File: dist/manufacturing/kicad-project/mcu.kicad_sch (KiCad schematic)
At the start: 22 parts, among them SW1 SW1, U16 STM32G0B1CBT6, U17 W25Q32JVSSIQ, Y1 Y1

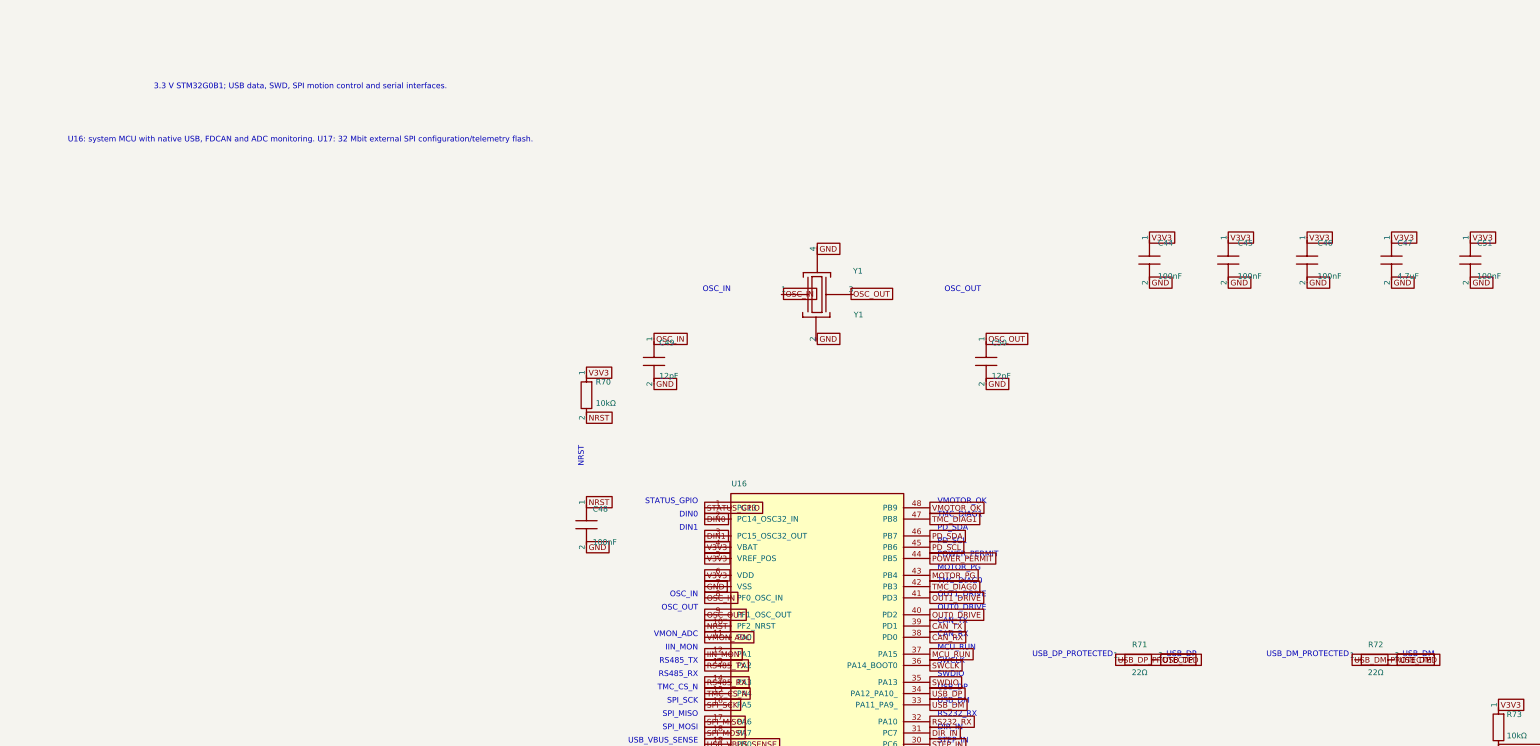
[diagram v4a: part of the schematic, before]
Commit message: Implement dual USB power/data ECO and consolidate industrial I/O
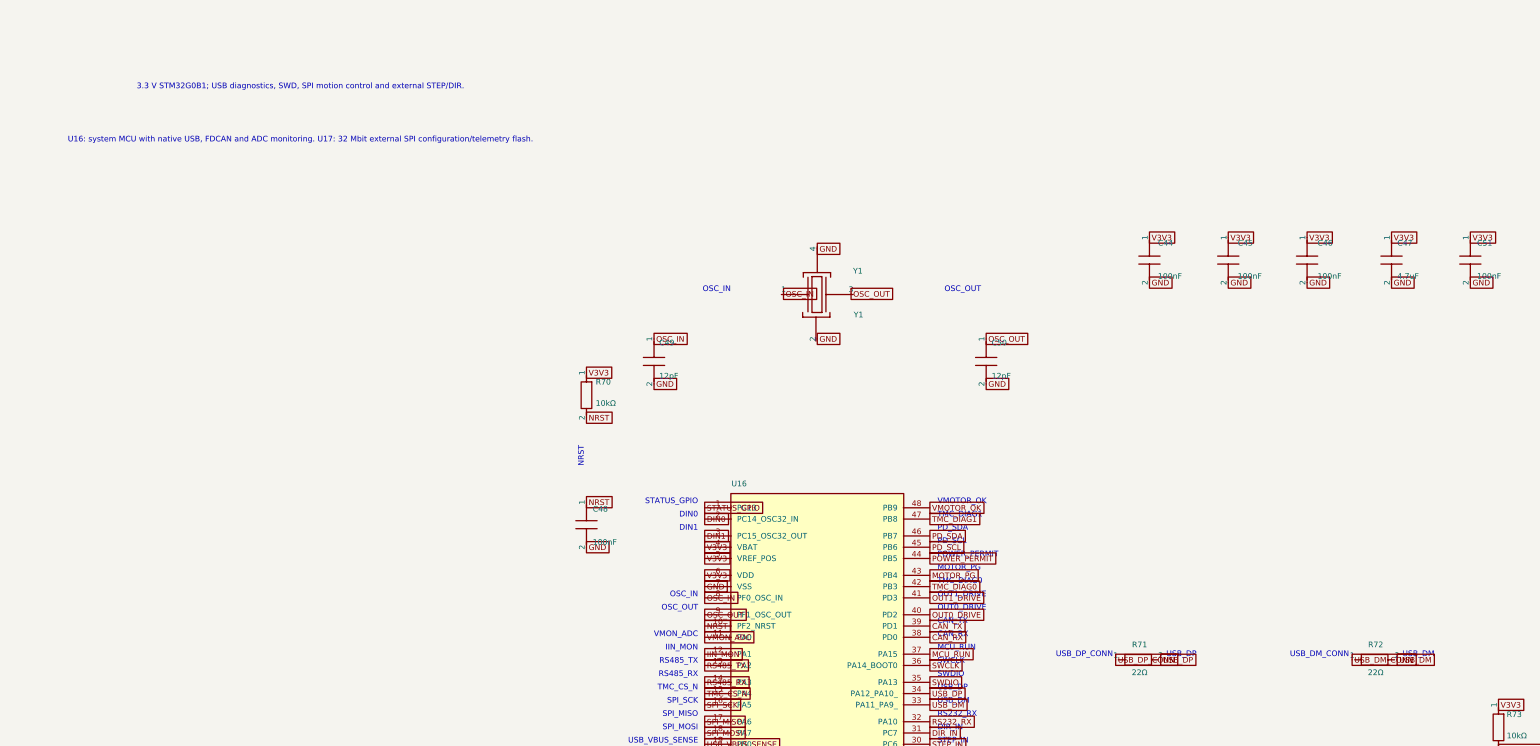
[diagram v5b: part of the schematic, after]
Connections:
- net USB_DM_PROTECTED renamed USB_DM_CONN
- net USB_DP_PROTECTED renamed USB_DP_CONN
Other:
- note added: "3.3 V STM32G0B1; USB diagnostics, SWD, SPI motion control and external STEP/DIR."
- note added: "USB_DM_CONN"
- note added: "USB_DP_CONN"
- note removed: "3.3 V STM32G0B1; USB data, SWD, SPI motion control and serial interfaces."
- note removed: "USB_DM_PROTECTED"
- note removed: "USB_DP_PROTECTED"
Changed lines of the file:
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@@
     (instances
       (project ""
-        (path "/93276a6d-ae71-49bc-84c0-d5988d306052/07041646-aaf2-45f7-ab53-7adcd4224a5f"
+        (path "/c498c7fb-1599-494d-ace0-607a3ed08d67/9503f2cd-f1e7-4884-9ff7-a57bb9d4f8c9"
           (reference "U16")
           (unit 1)
@@
     (instances
       (project ""
-        (path "/93276a6d-ae71-49bc-84c0-d5988d306052/07041646-aaf2-45f7-ab53-7adcd4224a5f"
+        (path "/c498c7fb-1599-494d-ace0-607a3ed08d67/9503f2cd-f1e7-4884-9ff7-a57bb9d4f8c9"
           (reference "C44")
           (unit 1)
@@
     (instances
       (project ""
-        (path "/93276a6d-ae71-49bc-84c0-d5988d306052/07041646-aaf2-45f7-ab53-7adcd4224a5f"
+        (path "/c498c7fb-1599-494d-ace0-607a3ed08d67/9503f2cd-f1e7-4884-9ff7-a57bb9d4f8c9"
           (reference "C45")
           (unit 1)
@@
     (instances
       (project ""
-        (path "/93276a6d-ae71-49bc-84c0-d5988d306052/07041646-aaf2-45f7-ab53-7adcd4224a5f"
+        (path "/c498c7fb-1599-494d-ace0-607a3ed08d67/9503f2cd-f1e7-4884-9ff7-a57bb9d4f8c9"
           (reference "C46")
           (unit 1)
@@
     (instances
       (project ""
-        (path "/93276a6d-ae71-49bc-84c0-d5988d306052/07041646-aaf2-45f7-ab53-7adcd4224a5f"
+        (path "/c498c7fb-1599-494d-ace0-607a3ed08d67/9503f2cd-f1e7-4884-9ff7-a57bb9d4f8c9"
           (reference "C47")
           (unit 1)
@@
     (instances
       (project ""
-        (path "/93276a6d-ae71-49bc-84c0-d5988d306052/07041646-aaf2-45f7-ab53-7adcd4224a5f"
+        (path "/c498c7fb-1599-494d-ace0-607a3ed08d67/9503f2cd-f1e7-4884-9ff7-a57bb9d4f8c9"
           (reference "R70")
           (unit 1)
@@
     (instances
       (project ""
-        (path "/93276a6d-ae71-49bc-84c0-d5988d306052/07041646-aaf2-45f7-ab53-7adcd4224a5f"
+        (path "/c498c7fb-1599-494d-ace0-607a3ed08d67/9503f2cd-f1e7-4884-9ff7-a57bb9d4f8c9"
           (reference "C48")
           (unit 1)
@@
     (instances
       (project ""
-        (path "/93276a6d-ae71-49bc-84c0-d5988d306052/07041646-aaf2-45f7-ab53-7adcd4224a5f"
+        (path "/c498c7fb-1599-494d-ace0-607a3ed08d67/9503f2cd-f1e7-4884-9ff7-a57bb9d4f8c9"
           (reference "R71")
           (unit 1)
@@
     (instances
       (project ""
-        (path "/93276a6d-ae71-49bc-84c0-d5988d306052/07041646-aaf2-45f7-ab53-7adcd4224a5f"
+        (path "/c498c7fb-1599-494d-ace0-607a3ed08d67/9503f2cd-f1e7-4884-9ff7-a57bb9d4f8c9"
           (reference "R72")
           (unit 1)
@@
     (instances
       (project ""
-        (path "/93276a6d-ae71-49bc-84c0-d5988d306052/07041646-aaf2-45f7-ab53-7adcd4224a5f"
+        (path "/c498c7fb-1599-494d-ace0-607a3ed08d67/9503f2cd-f1e7-4884-9ff7-a57bb9d4f8c9"
           (reference "Y1")
           (unit 1)
@@
     (instances
       (project ""
-        (path "/93276a6d-ae71-49bc-84c0-d5988d306052/07041646-aaf2-45f7-ab53-7adcd4224a5f"
+        (path "/c498c7fb-1599-494d-ace0-607a3ed08d67/9503f2cd-f1e7-4884-9ff7-a57bb9d4f8c9"
           (reference "C49")
           (unit 1)
@@
     (instances
       (project ""
-        (path "/93276a6d-ae71-49bc-84c0-d5988d306052/07041646-aaf2-45f7-ab53-7adcd4224a5f"
+        (path "/c498c7fb-1599-494d-ace0-607a3ed08d67/9503f2cd-f1e7-4884-9ff7-a57bb9d4f8c9"
           (reference "C50")
           (unit 1)
@@
     (instances
       (project ""
-        (path "/93276a6d-ae71-49bc-84c0-d5988d306052/07041646-aaf2-45f7-ab53-7adcd4224a5f"
+        (path "/c498c7fb-1599-494d-ace0-607a3ed08d67/9503f2cd-f1e7-4884-9ff7-a57bb9d4f8c9"
           (reference "SW1")
           (unit 1)
@@
     (instances
       (project ""
-        (path "/93276a6d-ae71-49bc-84c0-d5988d306052/07041646-aaf2-45f7-ab53-7adcd4224a5f"
+        (path "/c498c7fb-1599-494d-ace0-607a3ed08d67/9503f2cd-f1e7-4884-9ff7-a57bb9d4f8c9"
           (reference "TP_SWD_3V3")
           (unit 1)
@@
     (instances
       (project ""
-        (path "/93276a6d-ae71-49bc-84c0-d5988d306052/07041646-aaf2-45f7-ab53-7adcd4224a5f"
+        (path "/c498c7fb-1599-494d-ace0-607a3ed08d67/9503f2cd-f1e7-4884-9ff7-a57bb9d4f8c9"
           (reference "TP_SWDIO")
           (unit 1)
@@
     (instances
       (project ""
-        (path "/93276a6d-ae71-49bc-84c0-d5988d306052/07041646-aaf2-45f7-ab53-7adcd4224a5f"
+        (path "/c498c7fb-1599-494d-ace0-607a3ed08d67/9503f2cd-f1e7-4884-9ff7-a57bb9d4f8c9"
           (reference "TP_SWD_GND")
           (unit 1)
@@
     (instances
       (project ""
-        (path "/93276a6d-ae71-49bc-84c0-d5988d306052/07041646-aaf2-45f7-ab53-7adcd4224a5f"
+        (path "/c498c7fb-1599-494d-ace0-607a3ed08d67/9503f2cd-f1e7-4884-9ff7-a57bb9d4f8c9"
           (reference "TP_SWCLK")
           (unit 1)
@@
     (instances
       (project ""
-        (path "/93276a6d-ae71-49bc-84c0-d5988d306052/07041646-aaf2-45f7-ab53-7adcd4224a5f"
+        (path "/c498c7fb-1599-494d-ace0-607a3ed08d67/9503f2cd-f1e7-4884-9ff7-a57bb9d4f8c9"
           (reference "TP_NRST")
           (unit 1)
@@
     (instances
       (project ""
-        (path "/93276a6d-ae71-49bc-84c0-d5988d306052/07041646-aaf2-45f7-ab53-7adcd4224a5f"
+        (path "/c498c7fb-1599-494d-ace0-607a3ed08d67/9503f2cd-f1e7-4884-9ff7-a57bb9d4f8c9"
           (reference "TP_STATUS")
           (unit 1)
@@
     (instances
       (project ""
-        (path "/93276a6d-ae71-49bc-84c0-d5988d306052/07041646-aaf2-45f7-ab53-7adcd4224a5f"
+        (path "/c498c7fb-1599-494d-ace0-607a3ed08d67/9503f2cd-f1e7-4884-9ff7-a57bb9d4f8c9"
           (reference "U17")
           (unit 1)
@@
     (instances
       (project ""
-        (path "/93276a6d-ae71-49bc-84c0-d5988d306052/07041646-aaf2-45f7-ab53-7adcd4224a5f"
+        (path "/c498c7fb-1599-494d-ace0-607a3ed08d67/9503f2cd-f1e7-4884-9ff7-a57bb9d4f8c9"
           (reference "R73")
           (unit 1)
@@
     (instances
       (project ""
-        (path "/93276a6d-ae71-49bc-84c0-d5988d306052/07041646-aaf2-45f7-ab53-7adcd4224a5f"
+        (path "/c498c7fb-1599-494d-ace0-607a3ed08d67/9503f2cd-f1e7-4884-9ff7-a57bb9d4f8c9"
           (reference "C51")
           (unit 1)
@@
     )
   )
-  (text "3.3 V STM32G0B1; USB data, SWD, SPI motion control and serial interfaces."
+  (text "3.3 V STM32G0B1; USB diagnostics, SWD, SPI motion control and external STEP/DIR."
     (at 45.97500000000001 15.499999999999972 0)
     (effects
@@
     )
   )
-  (text "USB_DP_PROTECTED"
+  (text "USB_DP_CONN"
     (at 229.275 143.59999999999997 0)
     (effects
@@
     )
   )
-  (text "USB_DM_PROTECTED"
-    (at 282.525 143.59999999999997 0)
+  (text "USB_DM_CONN"
+    (at 282.52500000000003 143.59999999999997 0)
     (effects
       (font
@@
     (fields_autoplaced no)
   )
-  (global_label "USB_DP_PROTECTED"
+  (global_label "USB_DP_CONN"
     (shape passive)
     (at 229.87 144.78 0)
@@
     (fields_autoplaced no)
   )
-  (global_label "USB_DM_PROTECTED"
+  (global_label "USB_DM_CONN"
     (shape passive)
     (at 283.21000000000004 144.78 0)
